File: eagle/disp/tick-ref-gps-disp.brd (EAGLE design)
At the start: 81.3 x 106.3 mm, 37 parts, among them CN1 To Main Board, Q1 MMBT3904, U1 AS1115, U2 AS1115

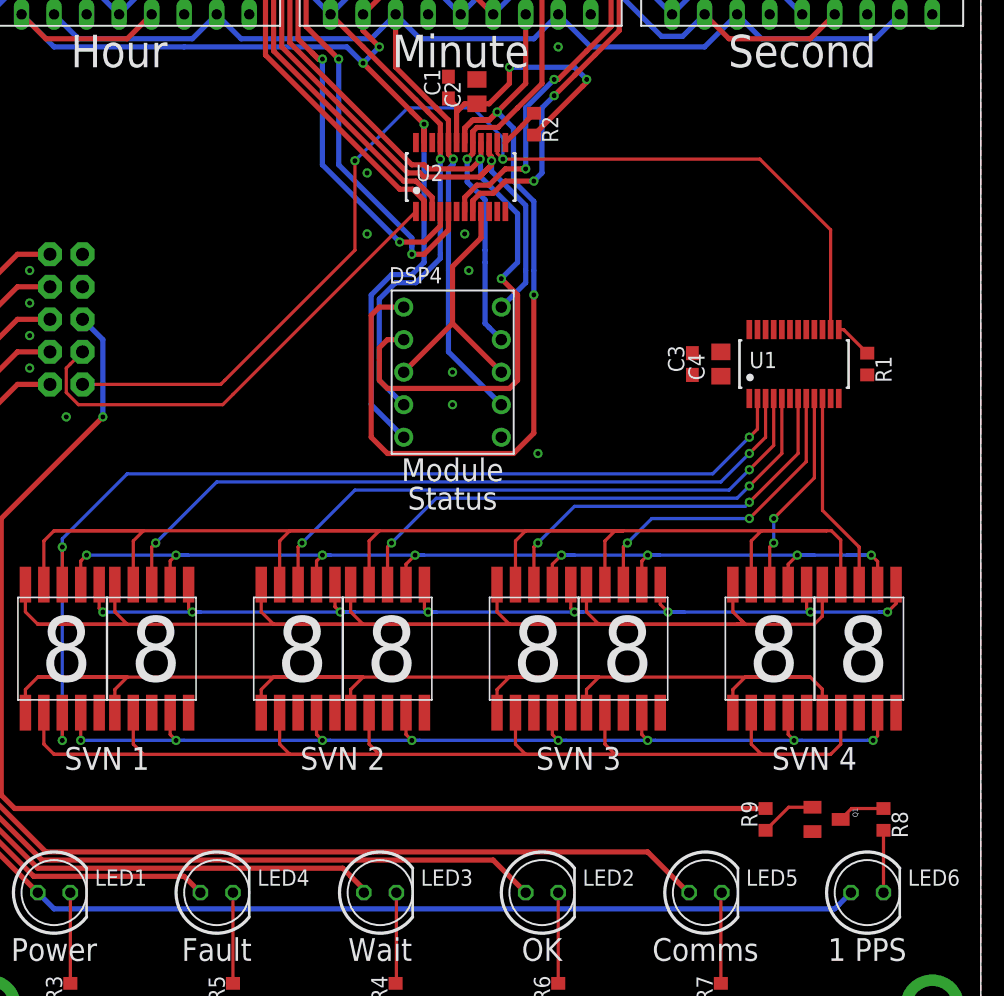
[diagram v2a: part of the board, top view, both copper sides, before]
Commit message: Completed routing, checklist still needs to be run-through and silkscreen needs to be finished.
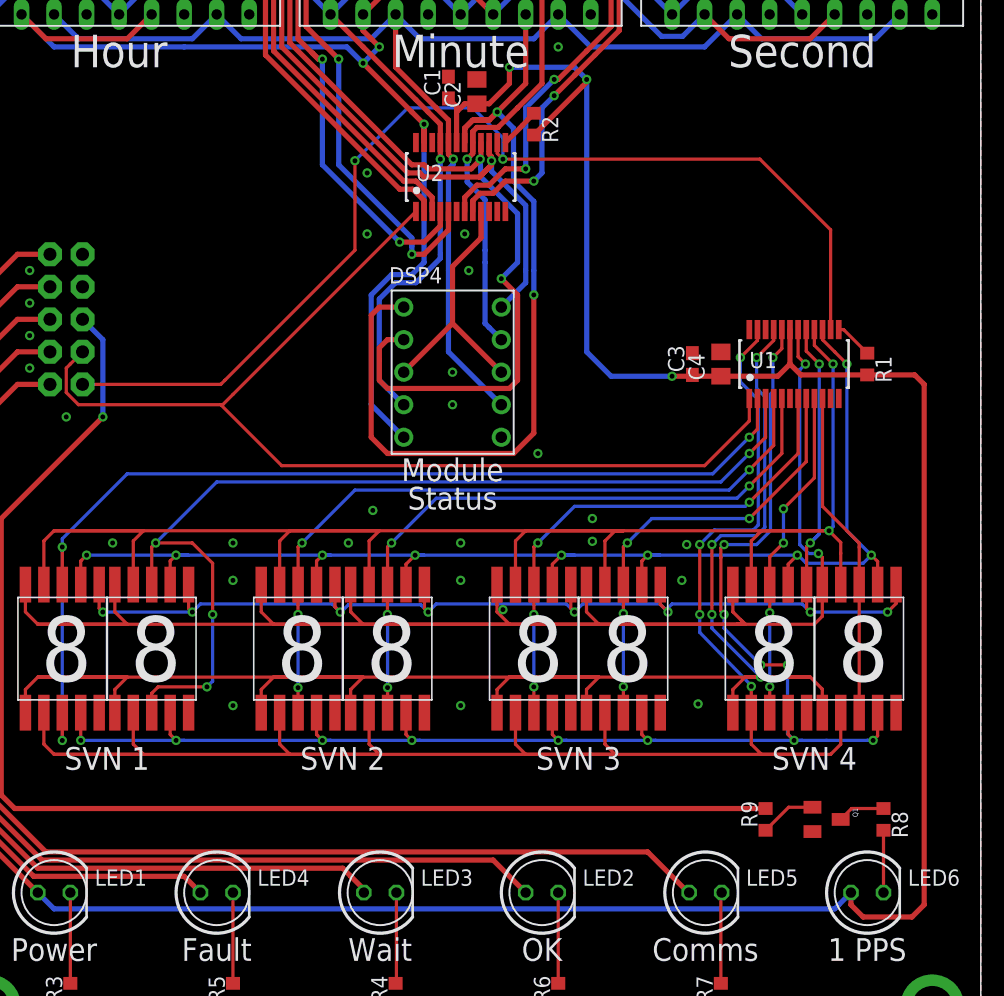
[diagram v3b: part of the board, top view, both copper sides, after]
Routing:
- net +5V: track 143.8 -> 244.2 mm, vias 2 -> 3
- net SDA: track 37.7 -> 84.1 mm
- net DSPB_SEG_C: track 84.7 -> 123.9 mm, vias 8 -> 13
- net DSPB_SEG_D: track 115.4 -> 151.7 mm, vias 0 -> 4
- net DSPB_SEG_E: track 111.8 -> 145.5 mm, vias 0 -> 4
- net DSP6-C: track 57.5 -> 79.2 mm, vias 2 -> 4
- net DSPB_SEG_G: track 133.4 -> 154.9 mm, vias 0 -> 2
- net DSPB_SEG_B: track 85.0 -> 104.5 mm, vias 8 -> 10
- net DSPB_SEG_F: track 124.3 -> 141.4 mm, vias 0 -> 2
- net DSPB_SEG_A: track 89.0 -> 105.5 mm, vias 8 -> 9
- net DSP9-C: track 30.9 -> 40.9 mm, vias 2 -> 4
- net DSP7-C: track 47.0 -> 57.0 mm, vias 2 -> 4
- net DSP8-C: track 41.1 -> 51.1 mm, vias 2 -> 4
- net DSP10-C: track 24.9 -> 34.9 mm, vias 2 -> 4
- net DSP11-C: track 16.0 -> 26.0 mm, vias 2 -> 4
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
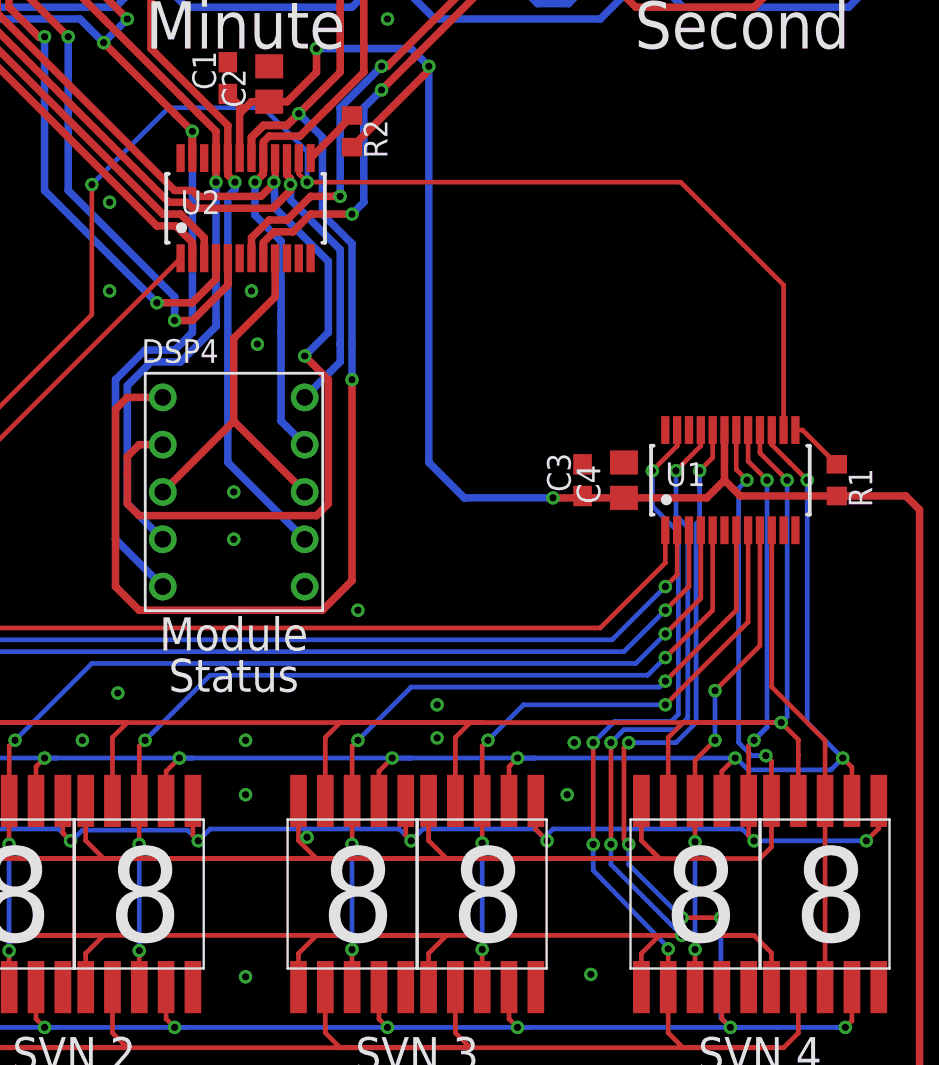
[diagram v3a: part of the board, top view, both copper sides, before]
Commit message: Fixed off-center status display.
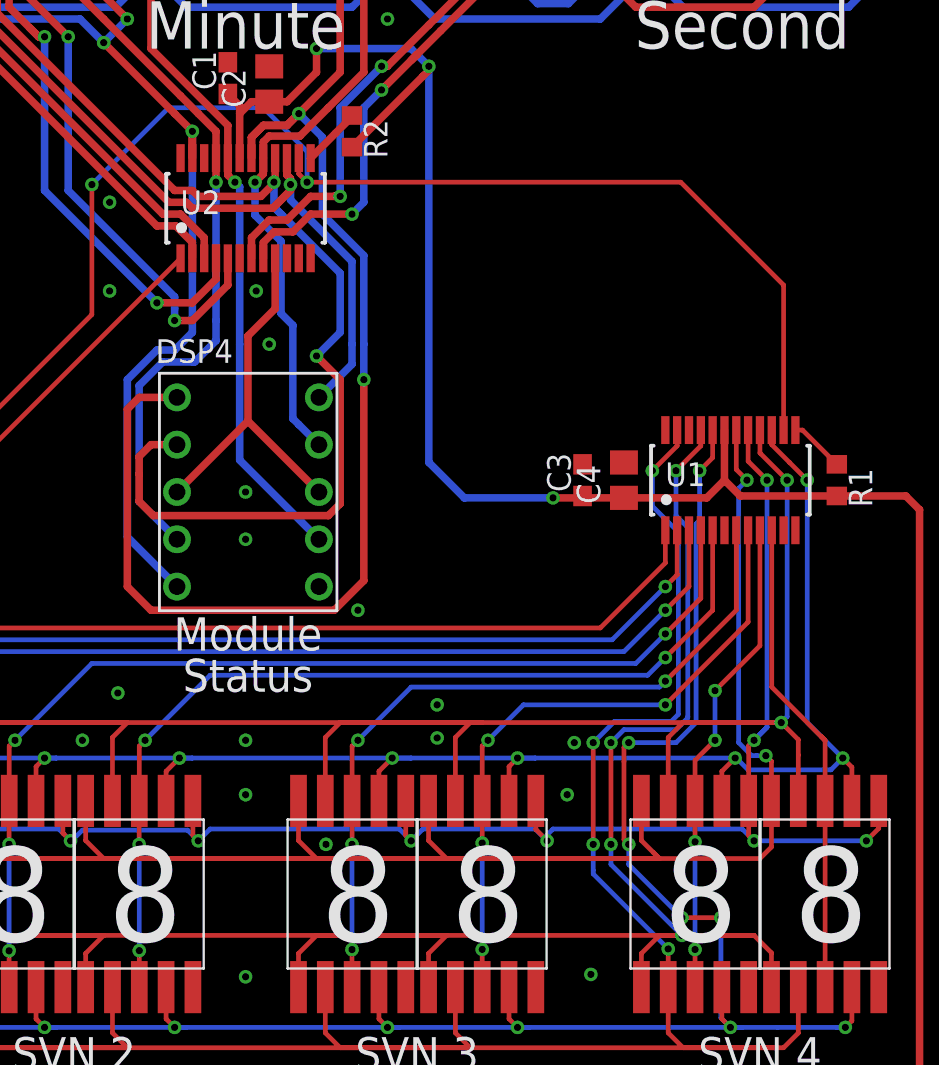
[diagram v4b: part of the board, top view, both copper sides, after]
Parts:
- moved DSP4 0.76 mm to (40.8, 53.3)
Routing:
- net DSPA_SEG_F: track 152.7 -> 153.6 mm
- net DSPA_SEG_D: track 125.6 -> 125.0 mm
